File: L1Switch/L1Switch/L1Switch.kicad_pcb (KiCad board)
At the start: 4 copper layers, 54 parts, among them J1 RJSNEGF8A08, J2 Conn_01x07_Male, T1 SM51589PEL, T2 SM51589PEL, U1 XC7A15T-FTG256, U2 VSC8658

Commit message: Add 1V2 power supply.
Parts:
- added C29: 22 uF, 3.637 mΩ, Capacitor_SMD:C_1206_3216Metric, F.Cu at (120.8, 3.96)
- added C30: 22 uF, 3.637 mΩ, Capacitor_SMD:C_1206_3216Metric, F.Cu at (120.8, 6.44)
- added C31: 22 uF, 3.637 mΩ, Capacitor_SMD:C_1206_3216Metric, F.Cu at (120.8, 8.92)
- added C32: 2.2 nF, 1.268 Ω, Capacitor_SMD:C_0402_1005Metric, F.Cu at (120.8, 1.75)
- added C33: 2.2 uF, 9.497 mΩ, Capacitor_SMD:C_0805_2012Metric, F.Cu at (125.4, -1.09)
- added C34: 2.2 uF, 9.497 mΩ, Capacitor_SMD:C_0805_2012Metric, F.Cu at (128.6, -1.80)
- added C35: 100 nF, 64 mOhm, Capacitor_SMD:C_0805_2012Metric, F.Cu at (114.4, -1.52)
- added C36: 470 pF, 5.548 Ω, Capacitor_SMD:C_0402_1005Metric, F.Cu at (110.4, -5.84)
- added C37: 100 uF, 4.885 mΩ, Capacitor_SMD:C_1206_3216Metric, F.Cu at (93.7, 8.00)
- added C38: 100 uF, 4.885 mΩ, Capacitor_SMD:C_1206_3216Metric, F.Cu at (90.0, 8.00)
- added C39: 100 uF, 4.885 mΩ, Capacitor_SMD:C_1206_3216Metric, F.Cu at (86.3, 8.00)
- added C40: 100 uF, 4.885 mΩ, Capacitor_SMD:C_1206_3216Metric, F.Cu at (82.6, 8.00)
- added C41: 100 uF, 4.885 mΩ, Capacitor_SMD:C_1206_3216Metric, F.Cu at (79.0, 8.00)
- added C42: 100 uF, 4.885 mΩ, Capacitor_SMD:C_1206_3216Metric, F.Cu at (75.3, 8.00)
- added L1: 1 uH, 3.5 mΩ, L1Switch:INDPM110100X400N, F.Cu at (105.7, 1.40)
- added R21: 1K0, Resistor_SMD:R_0402_1005Metric, F.Cu at (125.3, 23.9)
- added R22: 249K, Resistor_SMD:R_0402_1005Metric, F.Cu at (117.9, -5.74)
- added R23: 44K2, Resistor_SMD:R_0402_1005Metric, F.Cu at (118.9, -5.74)
- added R24: 105K, Resistor_SMD:R_0402_1005Metric, F.Cu at (115.9, -3.84)
- added R25: 150K, Resistor_SMD:R_0402_1005Metric, F.Cu at (123.0, -2.62)
- added R26: 68K1, Resistor_SMD:R_0402_1005Metric, F.Cu at (119.9, -5.74)
- added R27: 3R01, Resistor_SMD:R_0402_1005Metric, F.Cu at (113.3, -5.87)
- added R28: 10K, Resistor_SMD:R_0402_1005Metric, F.Cu at (121.9, -5.33)
- added R29: 10K, Resistor_SMD:R_0402_1005Metric, F.Cu at (123.0, -3.66)
- added U3: TPS548A20RVE, L1Switch:TPS548A20RVER, F.Cu at (119.5, -1.57)
- C11, C12, C13, C14, C15, C16, C17, C18, C19, C2, C20, C21, C22, C23, C24, C25, C26, C3, C4, C5, C6, C7, C8, C9: value 0.1uF -> 0.1 uF
- moved R17 8.18 mm to (128.2, 23.9)
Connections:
- U1 pad A1: Net-(U1-PadA1) -> GND
- U1 pad A11: Net-(U1-PadA11) -> GND
- U1 pad A16: Net-(U1-PadA16) -> +1V2
- U1 pad A6: Net-(U1-PadA6) -> +1V2
- U1 pad B13: Net-(U1-PadB13) -> +1V2
- U1 pad B3: Net-(U1-PadB3) -> +1V2
- U1 pad B8: Net-(U1-PadB8) -> GND
- U1 pad C10: Net-(U1-PadC10) -> +1V2
- U1 pad C15: Net-(U1-PadC15) -> GND
- U1 pad C5: Net-(U1-PadC5) -> GND
- U1 pad D12: Net-(U1-PadD12) -> GND
- U1 pad D2: Net-(U1-PadD2) -> GND
- U1 pad D7: Net-(U1-PadD7) -> +1V2
- U1 pad E10: Net-(U1-PadE10) -> +1V0
- U1 pad E14: Net-(U1-PadE14) -> +1V2
- U1 pad E4: Net-(U1-PadE4) -> +1V2
- U1 pad E9: Net-(U1-PadE9) -> GND
- U1 pad F1: Net-(U1-PadF1) -> +1V2
- U1 pad F10: Net-(U1-PadF10) -> GND
- U1 pad F11: Net-(U1-PadF11) -> +1V0
- U1 pad F16: Net-(U1-PadF16) -> GND
- U1 pad F6: Net-(U1-PadF6) -> GND
- U1 pad F7: Net-(U1-PadF7) -> +1V0
- U1 pad F8: Net-(U1-PadF8) -> +1V8
- U1 pad F9: Net-(U1-PadF9) -> +1V0
- U1 pad G10: Net-(U1-PadG10) -> +1V8
- U1 pad G13: Net-(U1-PadG13) -> GND
- U1 pad G3: Net-(U1-PadG3) -> GND
- U1 pad G6: Net-(U1-PadG6) -> +1V0
- U1 pad G7: Net-(U1-PadG7) -> GND
- U1 pad G8: Net-(U1-PadG8) -> +1V8
- U1 pad G9: Net-(U1-PadG9) -> GND
- U1 pad H15: Net-(U1-PadH15) -> +1V2
- U1 pad H6: Net-(U1-PadH6) -> GND
- U1 pad H9: Net-(U1-PadH9) -> +1V0
- U1 pad J10: Net-(U1-PadJ10) -> +1V8
- U1 pad J11: Net-(U1-PadJ11) -> GND
- U1 pad J12: Net-(U1-PadJ12) -> +1V2
- U1 pad J2: Net-(U1-PadJ2) -> +1V2
- U1 pad J6: Net-(U1-PadJ6) -> +1V0
- U1 pad J9: Net-(U1-PadJ9) -> GND
- U1 pad K11: Net-(U1-PadK11) -> +1V8
- U1 pad K14: Net-(U1-PadK14) -> GND
- U1 pad K4: Net-(U1-PadK4) -> GND
- U1 pad K6: Net-(U1-PadK6) -> GND
- U1 pad K9: Net-(U1-PadK9) -> +1V0
- U1 pad L1: Net-(U1-PadL1) -> GND
- U1 pad L10: Net-(U1-PadL10) -> +1V8
- U1 pad L11: Net-(U1-PadL11) -> GND
- U1 pad L16: Net-(U1-PadL16) -> +1V2
- U1 pad L4: Net-(U1-PadL4) -> /PHY_MDIO
- U1 pad L5: Net-(U1-PadL5) -> /PHY_MDC
- U1 pad L8: Net-(U1-PadL8) -> +1V0
- U1 pad M1: Net-(U1-PadM1) -> /PHY0_REFCLK
- U1 pad M13: Net-(U1-PadM13) -> +1V2
- U1 pad M2: Net-(U1-PadM2) -> /PHY_RESET_N
- U1 pad M3: Net-(U1-PadM3) -> +3V3
- U1 pad M4: Net-(U1-PadM4) -> /PHY_MDINT_N
- U1 pad M8: Net-(U1-PadM8) -> GND
- U1 pad N10: Net-(U1-PadN10) -> +1V2
- U1 pad N15: Net-(U1-PadN15) -> GND
- U1 pad N5: Net-(U1-PadN5) -> GND
- U1 pad P12: Net-(U1-PadP12) -> GND
- U1 pad P2: Net-(U1-PadP2) -> GND
- U1 pad P7: Net-(U1-PadP7) -> +1V2
- U1 pad R14: Net-(U1-PadR14) -> +1V2
- U1 pad R4: Net-(U1-PadR4) -> +3V3
- U1 pad R9: Net-(U1-PadR9) -> GND
- U1 pad T1: Net-(U1-PadT1) -> +3V3
- U1 pad T11: Net-(U1-PadT11) -> +1V2
- U1 pad T16: Net-(U1-PadT16) -> GND
- U1 pad T6: Net-(U1-PadT6) -> GND
- U2 pad J1: /PHY_REFCLK -> /PHY0_REFCLK
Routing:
- net +1V2: track 0.02 -> 30.9 mm, vias 0 -> 2
- net Net-(C33-Pad1): track 0.00 -> 21.2 mm
- net GND: track 178.3 -> 199.3 mm, vias 72 -> 105
- net Net-(R24-Pad2): track 0.00 -> 13.8 mm, vias 0 -> 2
- net Net-(C35-Pad1): track 0.00 -> 4.02 mm
- net Net-(C35-Pad2): track 0.00 -> 3.15 mm
- net Net-(R22-Pad2): track 0.00 -> 3.09 mm
- net Net-(R28-Pad2): track 0.00 -> 3.05 mm
- net /Power/VIN_5V: track 0.00 -> 2.91 mm
- net /Power/ENABLE_1V2: track 0.00 -> 2.41 mm, vias 0 -> 1
- net Net-(C36-Pad2): track 0.00 -> 1.86 mm
- net Net-(R26-Pad1): track 0.00 -> 1.55 mm
- net Net-(R25-Pad1): track 0.00 -> 1.49 mm
- added copper zone on F.Cu, net +1V2
- added copper zone on F.Cu, net /Power/VIN_5V
- added copper zone on F.Cu, net GND
- added copper zone on In1.Cu, net GND
- added copper zone on F.Cu, net Net-(C35-Pad2)

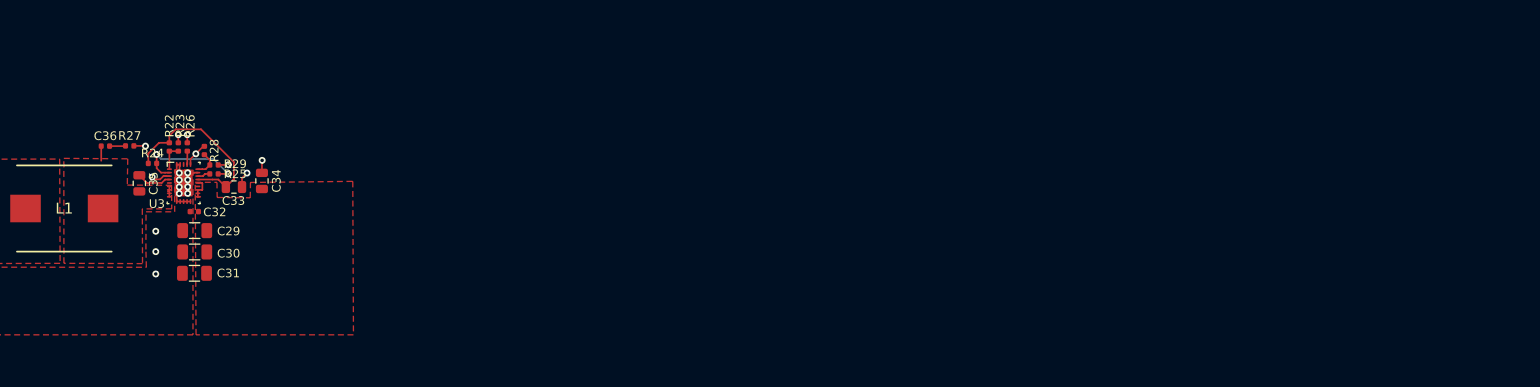
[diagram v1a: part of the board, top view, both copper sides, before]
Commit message: Added power supplies.
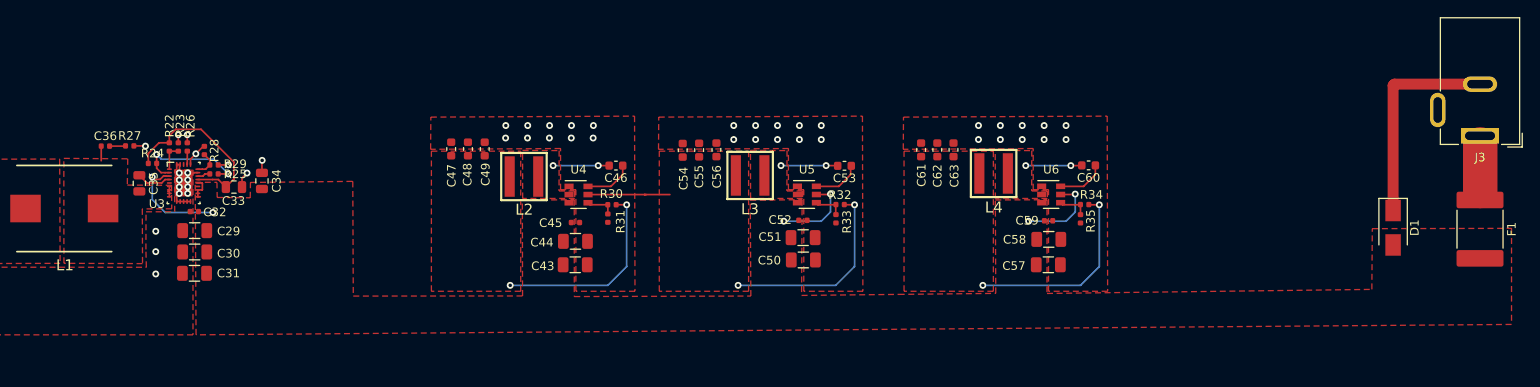
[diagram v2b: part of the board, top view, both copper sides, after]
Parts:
- added C43: 10 uF, 4.512 mΩ, Capacitor_SMD:C_1206_3216Metric, F.Cu at (164.9, 7.92)
- added C44: 10 uF, 4.512 mΩ, Capacitor_SMD:C_1206_3216Metric, F.Cu at (165.0, 5.21)
- added C45: 100 nF, 1 mΩ, Capacitor_SMD:C_0402_1005Metric, F.Cu at (165.0, 3.02)
- added C46: 100 nF, 1 mOhm, Capacitor_SMD:C_0603_1608Metric, F.Cu at (169.7, -3.58)
- added C47: 22 uF, 1 mΩ, Capacitor_SMD:C_0603_1608Metric, F.Cu at (150.6, -5.51)
- added C48: 22 uF, 1 mΩ, Capacitor_SMD:C_0603_1608Metric, F.Cu at (152.5, -5.51)
- added C49: 22 uF, 1 mΩ, Capacitor_SMD:C_0603_1608Metric, F.Cu at (154.4, -5.51)
- added C50: 10 uF, 4.512 mΩ, Capacitor_SMD:C_1206_3216Metric, F.Cu at (191.4, 7.37)
- added C51: 10 uF, 4.512 mΩ, Capacitor_SMD:C_1206_3216Metric, F.Cu at (191.4, 4.78)
- added C52: 100 nF, 1 mΩ, Capacitor_SMD:C_0402_1005Metric, F.Cu at (191.4, 2.77)
- added C53: 100 nF, 1 mOhm, Capacitor_SMD:C_0603_1608Metric, F.Cu at (196.2, -3.56)
- added C54: 22 uF, 1 mΩ, Capacitor_SMD:C_0603_1608Metric, F.Cu at (177.4, -5.36)
- added C55: 22 uF, 1 mΩ, Capacitor_SMD:C_0603_1608Metric, F.Cu at (179.3, -5.38)
- added C56: 22 uF, 1 mΩ, Capacitor_SMD:C_0603_1608Metric, F.Cu at (181.3, -5.41)
- added C57: 10 uF, 4.512 mΩ, Capacitor_SMD:C_1206_3216Metric, F.Cu at (219.8, 7.92)
- added C58: 10 uF, 4.512 mΩ, Capacitor_SMD:C_1206_3216Metric, F.Cu at (219.9, 4.98)
- added C59: 100 nF, 1 mΩ, Capacitor_SMD:C_0402_1005Metric, F.Cu at (219.9, 2.82)
- added C60: 100 nF, 1 mOhm, Capacitor_SMD:C_0603_1608Metric, F.Cu at (224.5, -3.61)
- added C61: 22 uF, 1 mΩ, Capacitor_SMD:C_0603_1608Metric, F.Cu at (205.1, -5.41)
- added C62: 22 uF, 1 mΩ, Capacitor_SMD:C_0603_1608Metric, F.Cu at (207.0, -5.41)
- added C63: 22 uF, 1 mΩ, Capacitor_SMD:C_0603_1608Metric, F.Cu at (208.8, -5.41)
- added D1: P4SMA6.8CA, Diode_SMD:D_SMA, F.Cu at (259.8, 3.63)
- added F1: 2920L700/12MR-A, Fuse:Fuse_2920_7451Metric, F.Cu at (269.9, 3.79)
- added J3: Barrel_Jack, L1Switch:MJ-179PH, F.Cu at (269.9, -7.04)
- added L2: 2.2 uH, 13.2 mΩ, L1Switch:XAL5030, F.Cu at (159.0, -2.31)
- added L3: 2.2 uH, 13.2 mΩ, L1Switch:XAL5030, F.Cu at (185.2, -2.44)
- added L4: 2.2 uH, 13.2 mΩ, L1Switch:XAL5030, F.Cu at (213.5, -2.67)
- added R30: 33K2, Resistor_SMD:R_0402_1005Metric, F.Cu at (169.2, 0.96)
- added R31: 10K, Resistor_SMD:R_0402_1005Metric, F.Cu at (168.7, 2.51)
- added R32: 13K7, Resistor_SMD:R_0402_1005Metric, F.Cu at (195.7, 0.94)
- added R33: 10K, Resistor_SMD:R_0402_1005Metric, F.Cu at (195.2, 2.59)
- added R34: 3K09, Resistor_SMD:R_0402_1005Metric, F.Cu at (224.1, 0.94)
- added R35: 10K, Resistor_SMD:R_0402_1005Metric, F.Cu at (223.6, 2.59)
- added U4: TPS565208, Package_TO_SOT_SMD:SOT-23-6, F.Cu at (165.3, -0.22)
- added U5: TPS565208, Package_TO_SOT_SMD:SOT-23-6, F.Cu at (191.8, -0.23)
- added U6: TPS565208, Package_TO_SOT_SMD:SOT-23-6, F.Cu at (220.2, -0.23)
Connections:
- U3 pad 3: /Power/ENABLE_1V2 -> /Power/VIN_5V
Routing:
- net +1V8: track 0.00 -> 32.5 mm, vias 0 -> 2
- net /Power/VIN_5V: track 2.91 -> 34.8 mm, vias 0 -> 6
- net GND: track 199.3 -> 224.0 mm, vias 105 -> 135
- net +1V0: track 0.00 -> 22.8 mm, vias 0 -> 2
- net +3V3: track 0.00 -> 22.8 mm, vias 0 -> 2
- net Net-(C60-Pad2): track 0.00 -> 6.50 mm, vias 0 -> 2
- net Net-(C53-Pad2): track 0.00 -> 6.50 mm, vias 0 -> 2
- net Net-(C46-Pad2): track 0.00 -> 6.50 mm, vias 0 -> 2
- net Net-(C60-Pad1): track 0.00 -> 5.64 mm
- net Net-(C53-Pad1): track 0.00 -> 5.64 mm
- net Net-(C46-Pad1): track 0.00 -> 5.64 mm
- net Net-(F1-Pad1): track 0.00 -> 5.41 mm
- net Net-(R32-Pad2): track 0.00 -> 3.46 mm
- net Net-(R30-Pad2): track 0.00 -> 3.46 mm
- net Net-(R34-Pad2): track 0.00 -> 3.46 mm
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- added copper zone on F.Cu, net +1V0
- added copper zone on F.Cu, net +1V8
- added copper zone on F.Cu, net +3V3
- added copper zone on F.Cu, net Net-(C46-Pad2)
- added copper zone on F.Cu, net Net-(C53-Pad2)
- added copper zone on F.Cu, net Net-(C60-Pad2)

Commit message: Kicad schema update.
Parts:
- added R36: 75R0, Resistor_SMD:R_0402_1005Metric, F.Cu at (88.5, 66.1)
- added R37: 75R0, Resistor_SMD:R_0402_1005Metric, F.Cu at (85.4, 61.5)
- added R38: 75R0, Resistor_SMD:R_0402_1005Metric, F.Cu at (89.1, 61.0)
- added R39: 75R0, Resistor_SMD:R_0402_1005Metric, F.Cu at (89.1, 59.9)
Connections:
- J1 pad 110: /Net 1/P1.LED1 -> Net-(J1-Pad110)
- J1 pad 112: /Net 1/P1.LED3 -> Net-(J1-Pad112)
- J1 pad 210: /Net 1/P2.LED1 -> Net-(J1-Pad210)
- J1 pad 212: /Net 1/P2.LED3 -> Net-(J1-Pad212)
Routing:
- net /Net 1/P1.LED3: track 109.7 -> 10.0 mm, vias 1 -> 0
- net Net-(J1-Pad112): track 0.00 -> 96.3 mm, vias 0 -> 1
- net /Net 1/P1.LED1: track 93.3 -> 7.68 mm, vias 1 -> 0
- net Net-(J1-Pad110): track 0.00 -> 84.7 mm, vias 0 -> 1
- net /Net 1/P2.LED3: track 87.7 -> 5.99 mm, vias 1 -> 0
- net Net-(J1-Pad212): track 0.00 -> 81.0 mm, vias 0 -> 1
- net Net-(J1-Pad210): track 0.00 -> 73.1 mm, vias 0 -> 1
- net /Net 1/P2.LED1: track 78.5 -> 6.22 mm, vias 1 -> 0
- net Net-(J2-Pad6): track 0.00 -> 17.7 mm, vias 0 -> 1
- net Net-(J2-Pad3): track 0.00 -> 17.6 mm, vias 0 -> 1
- net Net-(J2-Pad5): track 0.00 -> 15.6 mm
- net Net-(J2-Pad2): track 0.00 -> 14.8 mm
- net Net-(J2-Pad4): track 0.00 -> 13.6 mm
- net /Net 1/TXVA_N1: track 44.6 -> 45.4 mm
- net /Net 1/TXVA_P1: track 43.4 -> 44.2 mm
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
